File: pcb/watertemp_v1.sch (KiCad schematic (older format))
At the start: 25 parts, among them J1 CONN_02X10, U1 LPC11U24FBD48, U2 LP5907-Q1, U3 RN2483, U4 SHT21, U5 DS18B20, Y1 Crystal

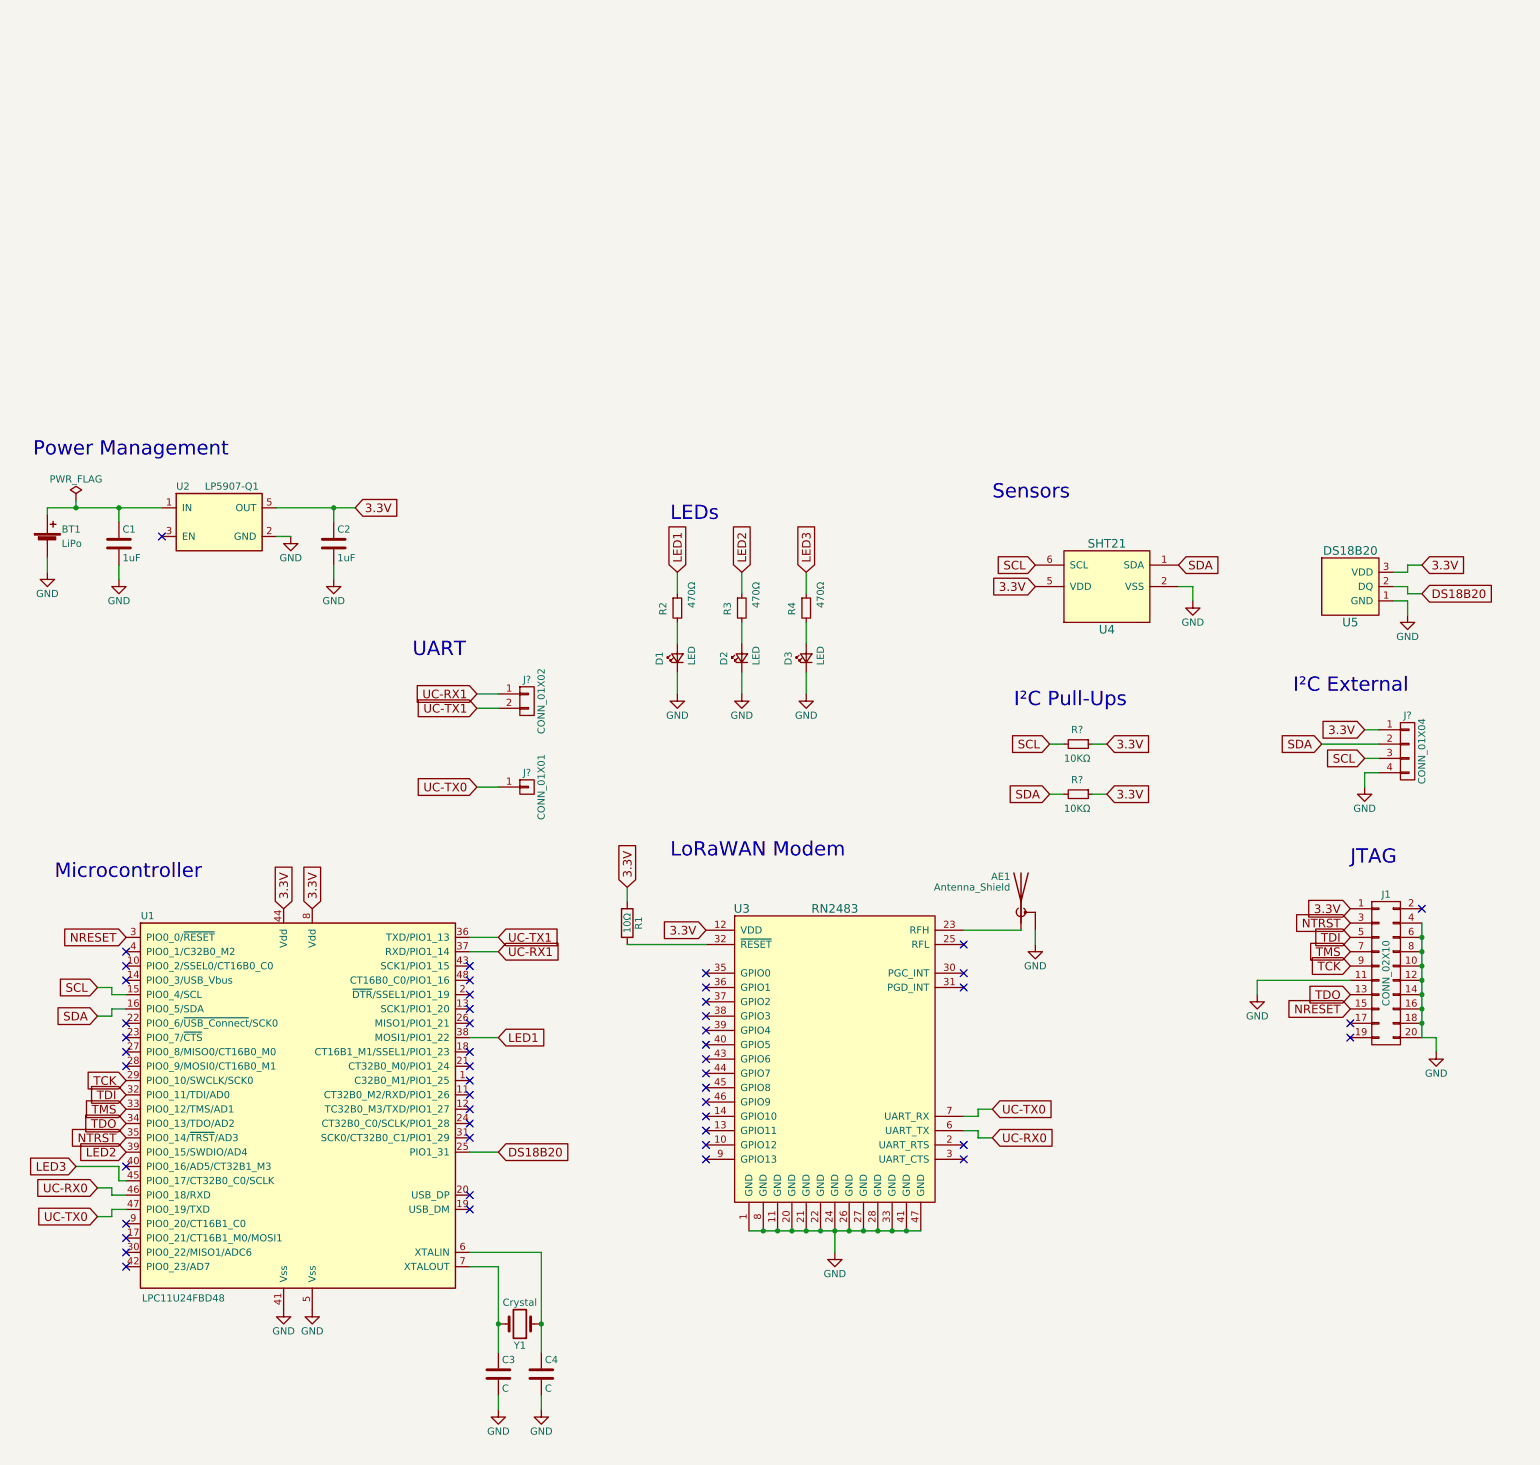
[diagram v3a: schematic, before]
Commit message: Add connector for external RN2483 board
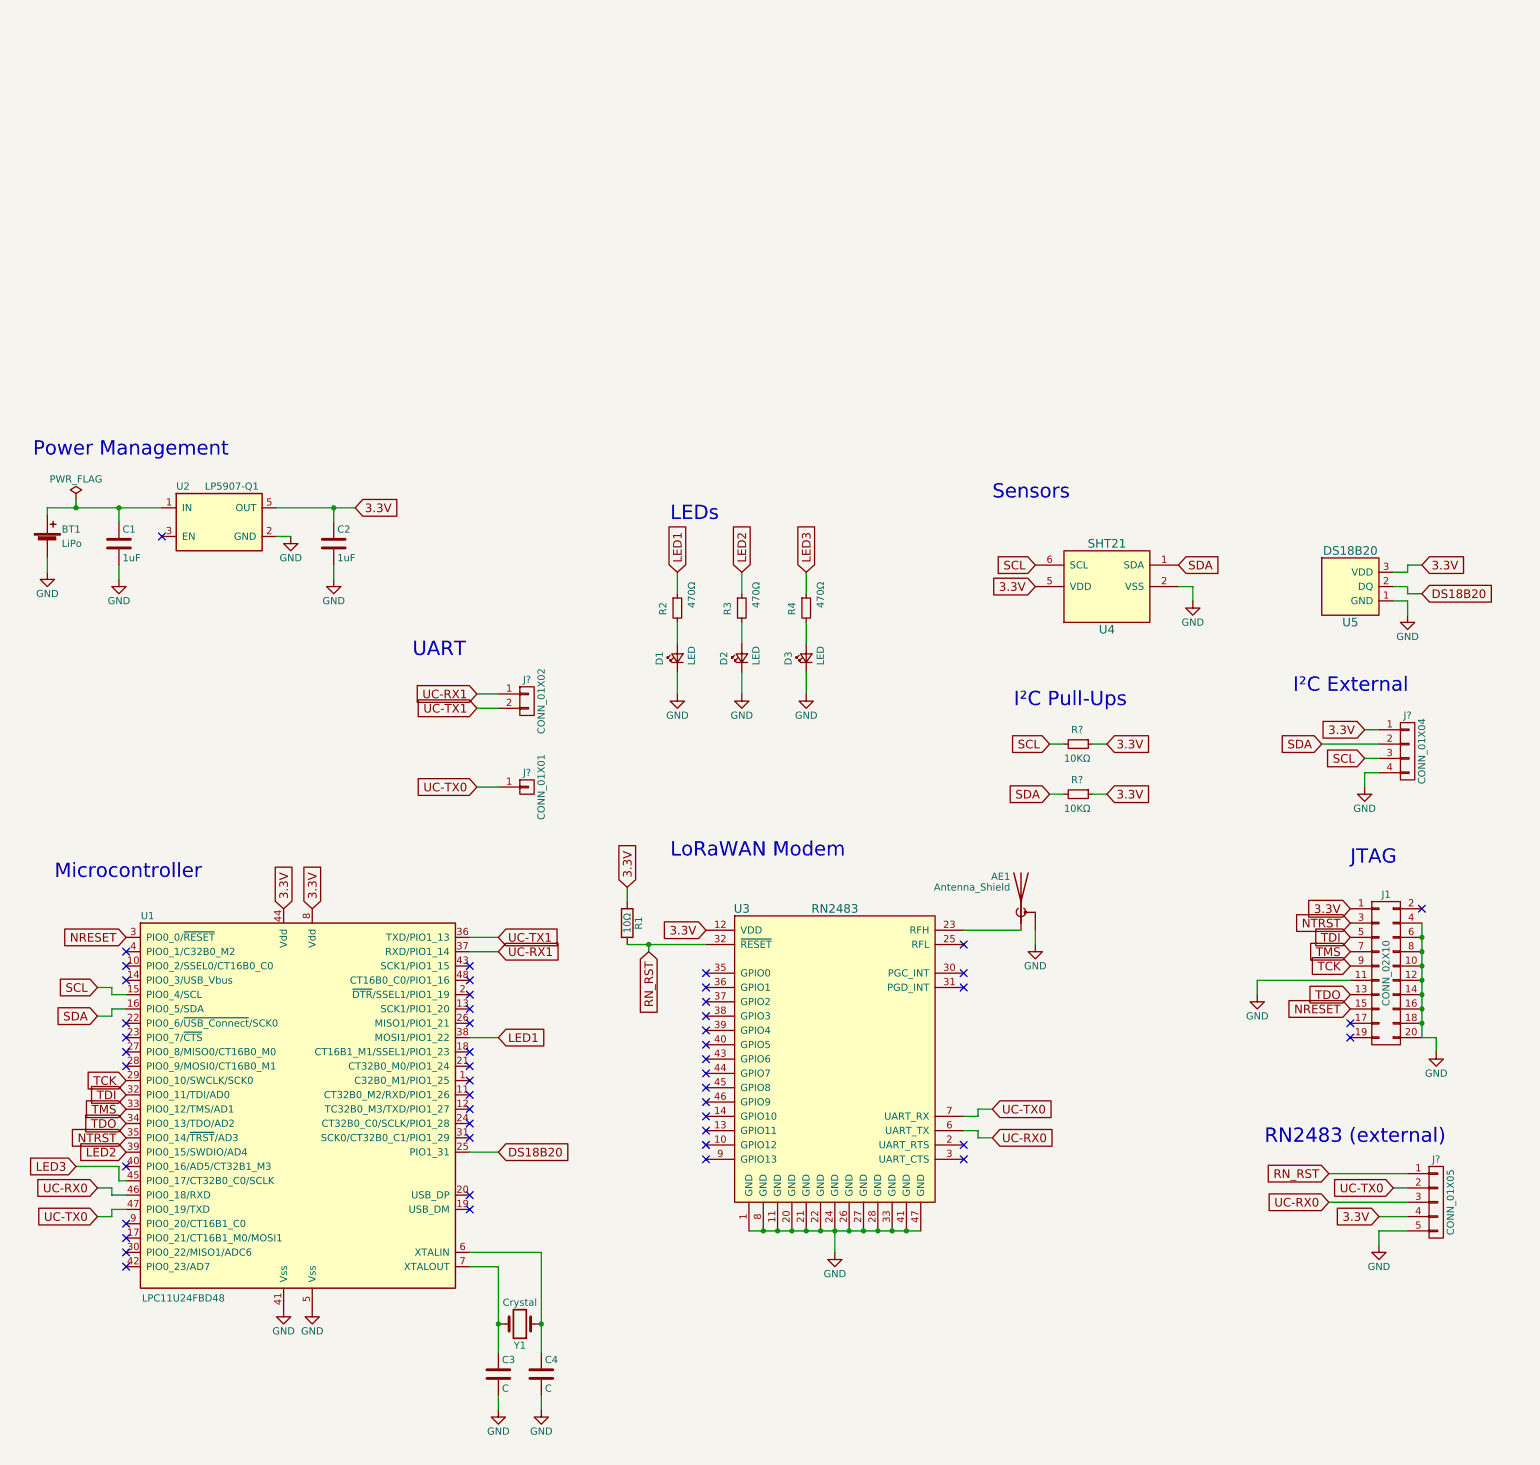
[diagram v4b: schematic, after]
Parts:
- added J?: CONN_01X05, symbol CONN_01X05
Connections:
- net 3.3V: now also J?.4 (P4)
- net GND: now also J?.5 (P5)
- net UC-RX0: now also J?.3 (P3)
- net UC-TX0: now also J?.2 (P2)
- net RN_RST: now reaches R1.2, U3.32 (~RESET)
- net RN_RST: now also J?.1 (P1)
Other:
- note added: "RN2483 (external)"
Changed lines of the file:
@@
 	7250 5450 7150 5450
 Wire Wire Line
-	5650 6150 6850 6150
+	5650 6150 5750 6150
+Wire Wire Line
+	5750 6150 5850 6150
+Wire Wire Line
+	5850 6150 5950 6150
+Wire Wire Line
+	5950 6150 6050 6150
+Wire Wire Line
+	6050 6150 6150 6150
+Wire Wire Line
+	6150 6150 6250 6150
+Wire Wire Line
+	6250 6150 6350 6150
+Wire Wire Line
+	6350 6150 6450 6150
+Wire Wire Line
+	6450 6150 6550 6150
+Wire Wire Line
+	6550 6150 6650 6150
+Wire Wire Line
+	6650 6150 6750 6150
+Wire Wire Line
+	6750 6150 6850 6150
 Connection ~ 5750 6150
 Connection ~ 5850 6150
@@
 	1200 6050 1100 6050
 Wire Wire Line
-	3900 6400 3900 7000
+	3900 6400 3900 6800
+Wire Wire Line
+	3900 6800 3900 7000
 Wire Wire Line
 	3900 6400 3700 6400
@@
 	3700 6300 4200 6300
 Wire Wire Line
-	4200 6300 4200 7000
+	4200 6300 4200 6800
+Wire Wire Line
+	4200 6800 4200 7000
 Connection ~ 3900 6800
 Connection ~ 4200 6800
@@
 	750  1150 750  1100
 Wire Wire Line
-	750  1100 1550 1100
-Wire Wire Line
-	2350 1100 2900 1100
+	750  1100 950  1100
+Wire Wire Line
+	950  1100 1250 1100
+Wire Wire Line
+	1250 1100 1550 1100
+Wire Wire Line
+	2350 1100 2750 1100
+Wire Wire Line
+	2750 1100 2900 1100
 Text GLabel 2900 1100 2    60   Input ~ 0
 3.3V
@@
 	10450 4800 10350 4800
 Wire Wire Line
-	10350 4800 10350 4000
+	10350 4800 10350 4700
+Wire Wire Line
+	10350 4700 10350 4600
+Wire Wire Line
+	10350 4600 10350 4500
+Wire Wire Line
+	10350 4500 10350 4400
+Wire Wire Line
+	10350 4400 10350 4300
+Wire Wire Line
+	10350 4300 10350 4200
+Wire Wire Line
+	10350 4200 10350 4100
+Wire Wire Line
+	10350 4100 10350 4000
 Connection ~ 10350 4700
 Connection ~ 10350 4600
@@
 $EndComp
 Wire Wire Line
-	5350 4150 4800 4150
+	5350 4150 4950 4150
+Wire Wire Line
+	4950 4150 4800 4150
 Wire Wire Line
 	4800 3750 4800 3850
@@
 Text GLabel 3750 3050 0    60   Input ~ 0
 UC-TX0
+Text Notes 9250 5550 0    100  ~ 0
+RN2483 (external)
+Wire Wire Line
+	10050 6150 10250 6150
+Wire Wire Line
+	10050 6150 10050 6250
+$Comp
+L GND #PWR?
+U 1 1 597403FE
+P 10050 6250
+F 0 "#PWR?" H 10050 6000 50  0001 C CNN
+F 1 "GND" H 10050 6100 50  0000 C CNN
+F 2 "" H 10050 6250 50  0001 C CNN
+F 3 "" H 10050 6250 50  0001 C CNN
+	1    10050 6250
+	1    0    0    -1
+$EndComp
+Text GLabel 10050 6050 0    60   Input ~ 0
+3.3V
+Text GLabel 10150 5850 0    60   Input ~ 0
+UC-TX0
+Text GLabel 9700 5950 0    60   Input ~ 0
+UC-RX0
+Wire Wire Line
+	9700 5950 10250 5950
+Wire Wire Line
+	10050 6050 10250 6050
+Text GLabel 4950 4200 3    60   Input ~ 0
+RN_RST
+Wire Wire Line
+	4950 4200 4950 4150
+Connection ~ 4950 4150
+Text GLabel 9700 5750 0    60   Input ~ 0
+RN_RST
+$Comp
+L CONN_01X05 J?
+U 1 1 597414DE
+P 10450 5950
+F 0 "J?" H 10450 6250 50  0000 C CNN
+F 1 "CONN_01X05" V 10550 5950 50  0000 C CNN
+F 2 "" H 10450 5950 50  0001 C CNN
+F 3 "" H 10450 5950 50  0001 C CNN
+	1    10450 5950
+	1    0    0    -1
+$EndComp
+Wire Wire Line
+	10150 5850 10250 5850
+Wire Wire Line
+	9700 5750 10250 5750
 $EndSCHEMATC

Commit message: Expose RN2483 ICSP header
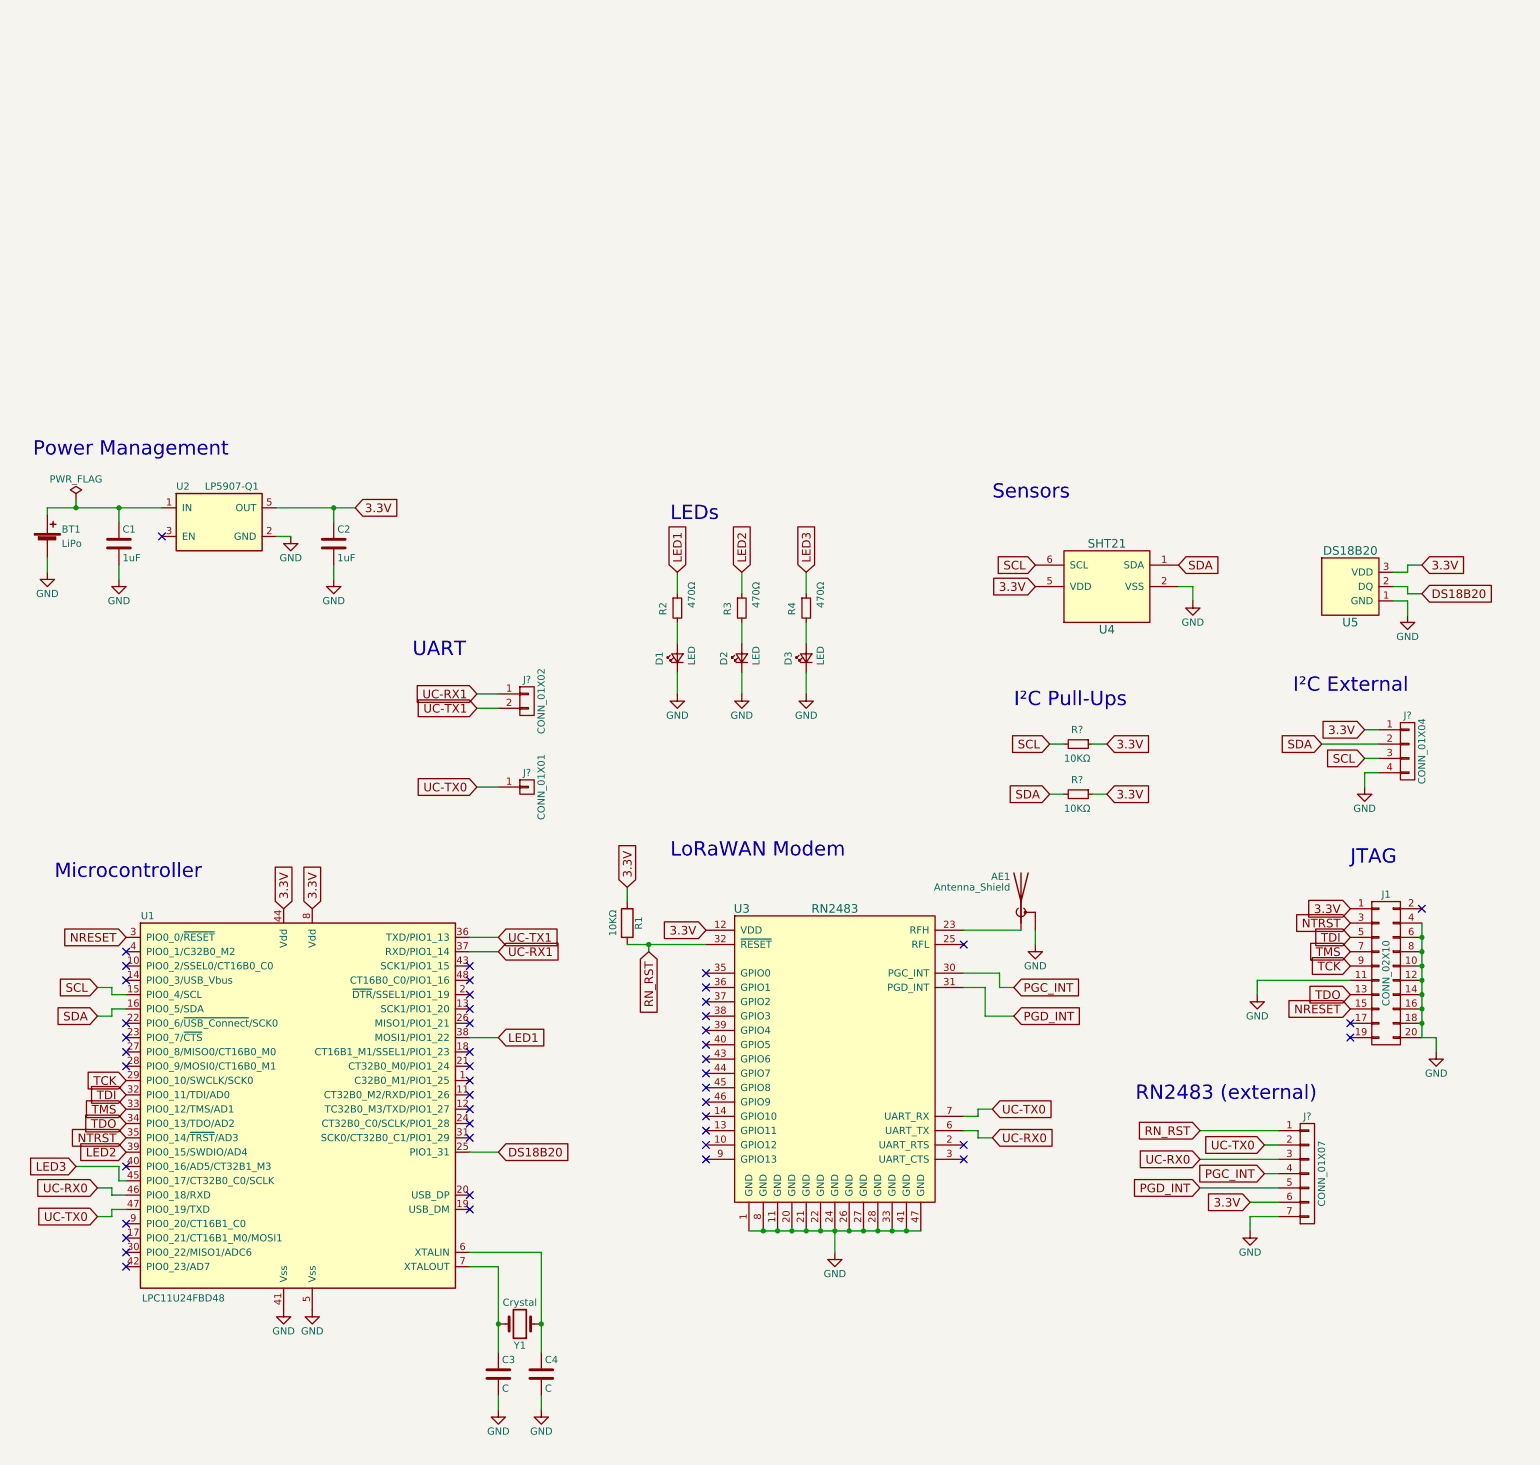
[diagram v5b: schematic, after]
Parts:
- removed J?: CONN_01X05, symbol CONN_01X05
- added J?: CONN_01X07, symbol CONN_01X07
- R1: value 10Ω -> 10KΩ
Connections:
- net 3.3V: now also J?.6 (P6)
- net GND: now also J?.7 (P7)
- net RN_RST: now also J?.1 (P1)
- net UC-RX0: now also J?.3 (P3)
- net UC-TX0: now also J?.2 (P2)
- net PGC_INT: now reaches U3.30 (PGC_INT)
- net PGC_INT: now also J?.4 (P4)
- net PGD_INT: now reaches U3.31 (PGD_INT)
- net PGD_INT: now also J?.5 (P5)
- no-connect marks 49 -> 47
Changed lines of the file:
@@
 	7250 5450 7150 5450
 Wire Wire Line
-	5650 6150 5750 6150
-Wire Wire Line
-	5750 6150 5850 6150
-Wire Wire Line
-	5850 6150 5950 6150
-Wire Wire Line
-	5950 6150 6050 6150
-Wire Wire Line
-	6050 6150 6150 6150
-Wire Wire Line
-	6150 6150 6250 6150
-Wire Wire Line
-	6250 6150 6350 6150
-Wire Wire Line
-	6350 6150 6450 6150
-Wire Wire Line
-	6450 6150 6550 6150
-Wire Wire Line
-	6550 6150 6650 6150
-Wire Wire Line
-	6650 6150 6750 6150
-Wire Wire Line
-	6750 6150 6850 6150
+	5650 6150 6850 6150
 Connection ~ 5750 6150
 Connection ~ 5850 6150
@@
 	1200 6050 1100 6050
 Wire Wire Line
-	3900 6400 3900 6800
-Wire Wire Line
-	3900 6800 3900 7000
+	3900 6400 3900 7000
 Wire Wire Line
 	3900 6400 3700 6400
@@
 	3700 6300 4200 6300
 Wire Wire Line
-	4200 6300 4200 6800
-Wire Wire Line
-	4200 6800 4200 7000
+	4200 6300 4200 7000
 Connection ~ 3900 6800
 Connection ~ 4200 6800
@@
 	750  1150 750  1100
 Wire Wire Line
-	750  1100 950  1100
-Wire Wire Line
-	950  1100 1250 1100
-Wire Wire Line
-	1250 1100 1550 1100
-Wire Wire Line
-	2350 1100 2750 1100
-Wire Wire Line
-	2750 1100 2900 1100
+	750  1100 1550 1100
+Wire Wire Line
+	2350 1100 2900 1100
 Text GLabel 2900 1100 2    60   Input ~ 0
 3.3V
@@
 	10450 4800 10350 4800
 Wire Wire Line
-	10350 4800 10350 4700
-Wire Wire Line
-	10350 4700 10350 4600
-Wire Wire Line
-	10350 4600 10350 4500
-Wire Wire Line
-	10350 4500 10350 4400
-Wire Wire Line
-	10350 4400 10350 4300
-Wire Wire Line
-	10350 4300 10350 4200
-Wire Wire Line
-	10350 4200 10350 4100
-Wire Wire Line
-	10350 4100 10350 4000
+	10350 4800 10350 4000
 Connection ~ 10350 4700
 Connection ~ 10350 4600
@@
 	1    0    0    -1
 $EndComp
-NoConn ~ 7150 4350
-NoConn ~ 7150 4450
 NoConn ~ 1300 4200
 NoConn ~ 1300 4300
@@
 P 4800 4000
 F 0 "R1" V 4880 4000 50  0000 C CNN
-F 1 "10Ω" V 4800 4000 50  0000 C CNN
+F 1 "10KΩ" V 4700 4000 50  0000 C CNN
 F 2 "" V 4730 4000 50  0001 C CNN
 F 3 "" H 4800 4000 50  0001 C CNN
@@
 $EndComp
 Wire Wire Line
-	5350 4150 4950 4150
-Wire Wire Line
-	4950 4150 4800 4150
+	4800 4150 5350 4150
 Wire Wire Line
 	4800 3750 4800 3850
@@
 Text GLabel 3750 3050 0    60   Input ~ 0
 UC-TX0
-Text Notes 9250 5550 0    100  ~ 0
+Text Notes 8350 5250 0    100  ~ 0
 RN2483 (external)
 Wire Wire Line
-	10050 6150 10250 6150
-Wire Wire Line
-	10050 6150 10050 6250
+	9150 6050 9350 6050
+Wire Wire Line
+	9150 6050 9150 6150
 $Comp
 L GND #PWR?
 U 1 1 597403FE
-P 10050 6250
-F 0 "#PWR?" H 10050 6000 50  0001 C CNN
-F 1 "GND" H 10050 6100 50  0000 C CNN
-F 2 "" H 10050 6250 50  0001 C CNN
-F 3 "" H 10050 6250 50  0001 C CNN
-	1    10050 6250
-	1    0    0    -1
-$EndComp
-Text GLabel 10050 6050 0    60   Input ~ 0
-3.3V
-Text GLabel 10150 5850 0    60   Input ~ 0
+P 9150 6150
+F 0 "#PWR?" H 9150 5900 50  0001 C CNN
+F 1 "GND" H 9150 6000 50  0000 C CNN
+F 2 "" H 9150 6150 50  0001 C CNN
+F 3 "" H 9150 6150 50  0001 C CNN
+	1    9150 6150
+	1    0    0    -1
+$EndComp
+Text GLabel 9150 5950 0    60   Input ~ 0
+3.3V
+Text GLabel 9250 5550 0    60   Input ~ 0
 UC-TX0
-Text GLabel 9700 5950 0    60   Input ~ 0
+Text GLabel 8800 5650 0    60   Input ~ 0
 UC-RX0
 Wire Wire Line
-	9700 5950 10250 5950
-Wire Wire Line
-	10050 6050 10250 6050
+	8800 5650 9350 5650
+Wire Wire Line
+	9150 5950 9350 5950
 Text GLabel 4950 4200 3    60   Input ~ 0
 RN_RST
@@
 	4950 4200 4950 4150
 Connection ~ 4950 4150
-Text GLabel 9700 5750 0    60   Input ~ 0
+Text GLabel 8800 5450 0    60   Input ~ 0
 RN_RST
-$Comp
-L CONN_01X05 J?
-U 1 1 597414DE
-P 10450 5950
-F 0 "J?" H 10450 6250 50  0000 C CNN
-F 1 "CONN_01X05" V 10550 5950 50  0000 C CNN
-F 2 "" H 10450 5950 50  0001 C CNN
-F 3 "" H 10450 5950 50  0001 C CNN
-	1    10450 5950
-	1    0    0    -1
-$EndComp
-Wire Wire Line
-	10150 5850 10250 5850
-Wire Wire Line
-	9700 5750 10250 5750
+Wire Wire Line
+	9250 5550 9350 5550
+Wire Wire Line
+	8800 5450 9350 5450
+$Comp
+L CONN_01X07 J?
+U 1 1 59742A19
+P 9550 5750
+F 0 "J?" H 9550 6150 50  0000 C CNN
+F 1 "CONN_01X07" V 9650 5750 50  0000 C CNN
+F 2 "" H 9550 5750 50  0001 C CNN
+F 3 "" H 9550 5750 50  0001 C CNN
+	1    9550 5750
+	1    0    0    -1
+$EndComp
+Text GLabel 9250 5750 0    60   Input ~ 0
+PGC_INT
+Text GLabel 8800 5850 0    60   Input ~ 0
+PGD_INT
+Wire Wire Line
+	9250 5750 9350 5750
+Wire Wire Line
+	8800 5850 9350 5850
+Text GLabel 7500 4450 2    60   Input ~ 0
+PGC_INT
+Text GLabel 7500 4650 2    60   Input ~ 0
+PGD_INT
+Wire Wire Line
+	7500 4450 7400 4450
+Wire Wire Line
+	7400 4450 7400 4350
+Wire Wire Line
+	7400 4350 7150 4350
+Wire Wire Line
+	7150 4450 7300 4450
+Wire Wire Line
+	7300 4450 7300 4650
+Wire Wire Line
+	7300 4650 7500 4650
 $EndSCHEMATC
